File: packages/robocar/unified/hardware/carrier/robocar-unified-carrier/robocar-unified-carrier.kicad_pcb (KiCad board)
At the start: 2 copper layers, 100 x 100 mm, 38 parts, among them J1 IDC 2x7 head cable, J10 Piezo, J2 IDC 2x7 head cable, J3 XT30 pack in, J4 LM2596 module, J5 Motor left, J6 Motor right, J7 RCWL-1601 front, J8 RCWL-1601 rear, J9 SSD1306 0.91in, U1 XIAO ESP32-S3 Sense, U2 AMS1117-3.3

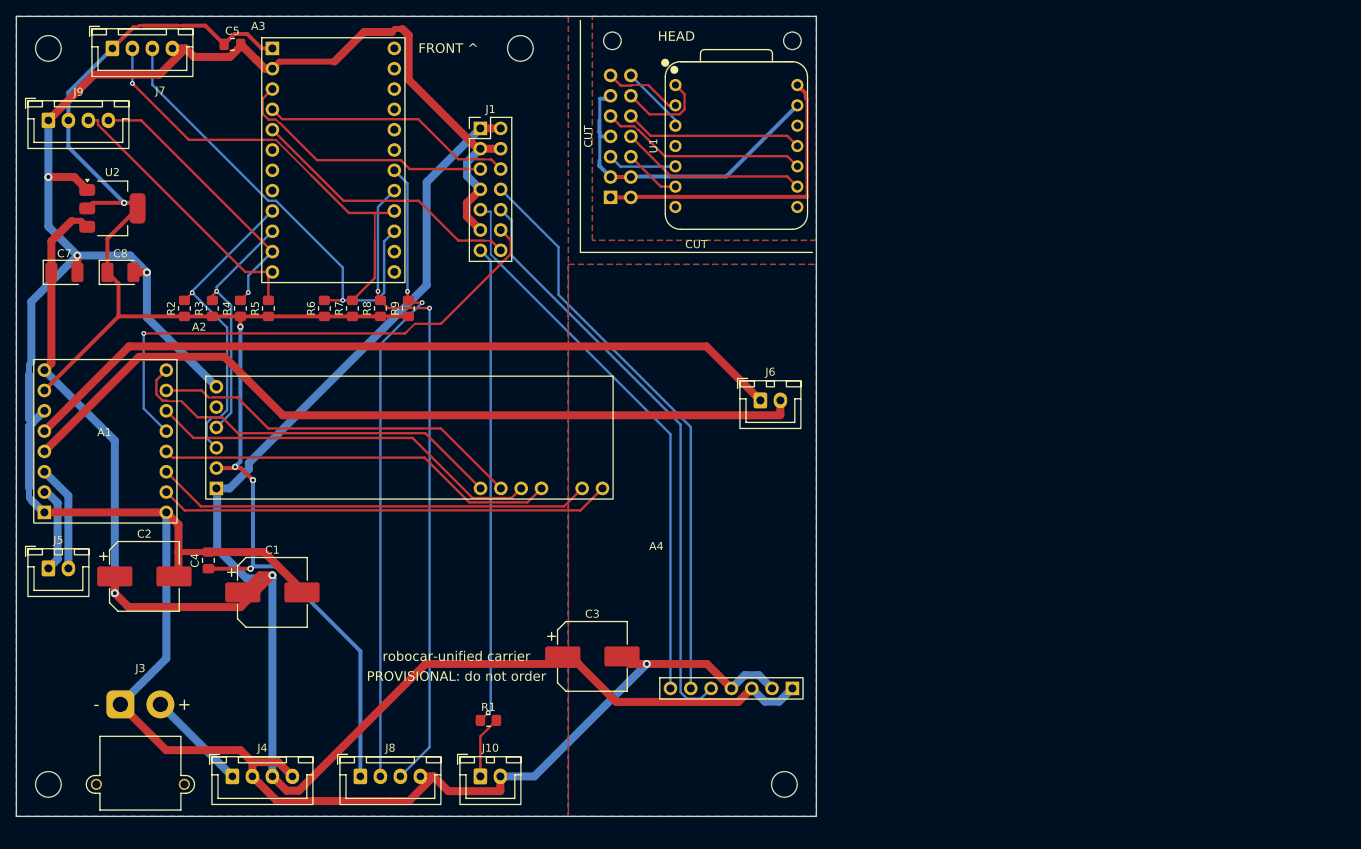
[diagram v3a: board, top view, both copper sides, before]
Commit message: feat(robocar-unified): carrier pre-order changes and three-head panel (#802)
* feat(kicad): circular board cutouts from board.toml [[cutouts]]

robocar-unified's head is sawn off the main board along an L-shaped line
(#750), and a hand saw cannot turn a sharp inside corner: the blade binds and
the corner cracks. A small hole at the corner gives the blade room to turn,
so board.toml needs a way to put a hole through the board. Its copper keepout
band forbids footprints, so the hole is board geometry, not a part.

- board.toml [[cutouts]]: { name, center = [x, y], diameter }, positions
  relative to the outline's top-left corner. boardcheck rejects a missing or
  repeated name, a bad centre or diameter, unknown keys, and a circle that
  is not strictly inside the outline (one touching it would open the edge).
- boardinput passes them through; build_board.py draws each as a circle on
  Edge.Cuts. KiCad's Specctra export then carries the hole as a keepout
  polygon on every signal layer, with the boundary still the outline
  rectangle, so Freerouting routes around it; a test pins both, and fails
  with the drawing removed.

balancebot's board.toml has no cutouts: its DSN export still equals the
fixture.

Co-Authored-By: Claude Opus 5.5 <noreply@anthropic.com>
Claude-Session: https://claude.ai/code/session_01LmLtwHDbHDLXFMLxCn3smf

* feat(parts): reversal-safe head ribbon pinout, UART0 TX carried to a tap

The head ribbon plugs onto unshrouded 2x7 pin headers, so its IDC plug also
fits rotated 180 degrees, which takes pin n to pin 15 - n. With the old
order that put 5 V on XIAO GPIOs. The new order (Lauri, 2026-10-16) pairs
each pin with one that is safe to swap with it:

  (1,14) 5V/5V  (2,13) GND/GND  (3,12) BCLK/LRC  (4,11) STBY/MUX_RST
  (5,10) SCL/SDA  (6,9) UART0 TX/NC  (7,8) DIN/PIEZO

Every non-I2C signal is a XIAO output driving a main-board input, so a
reversed plug only swaps outputs between inputs; I2C swaps with itself, and
TX lands on the unconnected pin 9.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
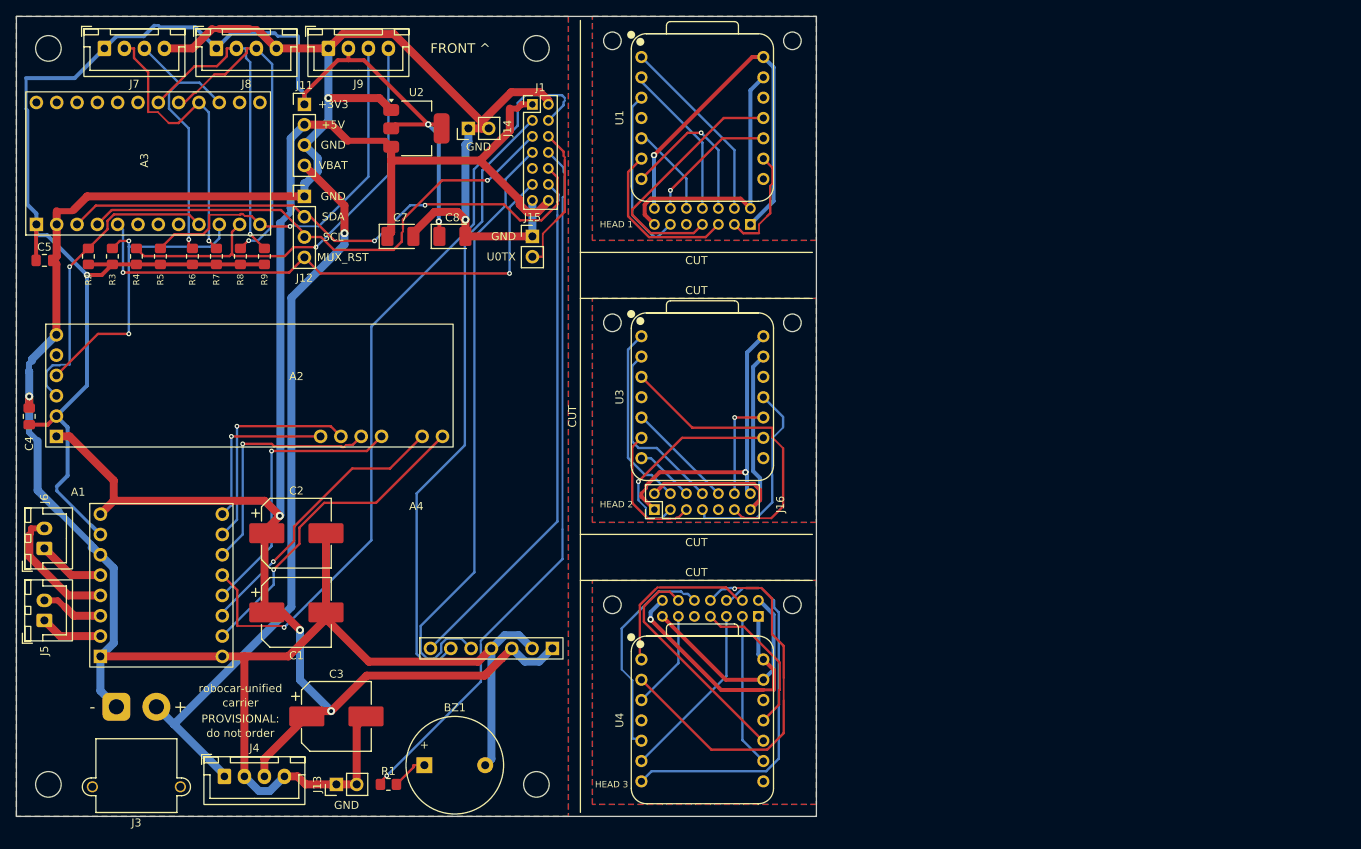
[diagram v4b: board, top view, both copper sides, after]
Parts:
- removed J10: Piezo, Connector_JST:JST_XH_B2B-XH-A_1x02_P2.50mm_Vertical
- added BZ1: Buzzer 12mm, Buzzer_Beeper:Buzzer_12x9.5RM7.6, F.Cu at (151.0, 193.6)
- added H10: M2, MountingHole:MountingHole_2.2mm_M2_ISO7380, F.Cu at (197.0, 173.6)
- added H7: M2, MountingHole:MountingHole_2.2mm_M2_ISO7380, F.Cu at (174.5, 138.3)
- added H8: M2, MountingHole:MountingHole_2.2mm_M2_ISO7380, F.Cu at (197.0, 138.3)
- added H9: M2, MountingHole:MountingHole_2.2mm_M2_ISO7380, F.Cu at (174.5, 173.6)
- added J11: Test: 3V3 5V GND VBAT, Connector_PinHeader_2.54mm:PinHeader_1x04_P2.54mm_Vertical, F.Cu at (136.0, 111.0)
- added J12: Test: GND SDA SCL RST, Connector_PinHeader_2.54mm:PinHeader_1x04_P2.54mm_Vertical, F.Cu at (136.0, 122.5)
- added J13: GND post, Connector_PinHeader_2.54mm:PinHeader_1x02_P2.54mm_Vertical, F.Cu at (140.0, 196.0)
- added J14: GND post, Connector_PinHeader_2.54mm:PinHeader_1x02_P2.54mm_Vertical, F.Cu at (156.5, 114.0)
- added J15: UART0 TX tap, Connector_PinHeader_2.54mm:PinHeader_1x02_P2.54mm_Vertical, F.Cu at (164.5, 127.5)
- added J16: IDC 2x7 head cable, Connector_PinHeader_2.00mm:PinHeader_2x07_P2.00mm_Vertical, F.Cu at (179.8, 161.7)
- added J17: IDC 2x7 head cable, Connector_PinHeader_2.00mm:PinHeader_2x07_P2.00mm_Vertical, B.Cu at (192.8, 175.0)
- added U3: XIAO ESP32-S3 Sense, Seeed_XIAO:XIAO-ESP32-S3-Socket, F.Cu at (185.8, 147.6)
- added U4: XIAO ESP32-S3 Sense, Seeed_XIAO:XIAO-ESP32-S3-Socket, F.Cu at (185.8, 188.0)
- H5, H6: footprint MountingHole:MountingHole_2.2mm_M2 -> MountingHole:MountingHole_2.2mm_M2_ISO7380
- J1, J2: footprint Connector_PinHeader_2.54mm:PinHeader_2x07_P2.54mm_Vertical -> Connector_PinHeader_2.00mm:PinHeader_2x07_P2.00mm_Vertical
- moved J8 92.8 mm to (125.0, 104.0)
- moved J6 91.4 mm to (103.5, 166.5), turned to 90 degrees
- moved C7 42.2 mm to (148.0, 127.5)
- moved C8 41.7 mm to (154.5, 127.5)
- moved U2 39.3 mm to (150.0, 114.0)
- moved A3 36.8 mm to (102.5, 126.0), turned to 90 degrees
- moved J9 36.1 mm to (139.0, 104.0)
- moved C5 35.8 mm to (103.5, 130.5)
- moved C3 32.9 mm to (140.0, 187.5)
- moved H4 31.0 mm to (165.0, 196.0)
- moved A4 30.4 mm to (167.0, 179.0)
- moved C4 28.7 mm to (101.6, 150.0)
- moved A2 21.0 mm to (105.0, 152.5)
- moved C2 19.8 mm to (135.0, 164.6)
- moved A1 19.3 mm to (110.5, 180.0)
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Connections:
- J1 pad 10: I2S_DIN -> I2C_SDA
- J1 pad 11: GND -> MUX_RST
- J1 pad 12: MOTOR_STBY -> I2S_LRCLK
- J1 pad 13: PIEZO -> GND
- J1 pad 14: MUX_RST -> +5V
- J1 pad 2: +5V -> GND
- J1 pad 3: GND -> I2S_BCLK
- J1 pad 4: GND -> MOTOR_STBY
- J1 pad 5: I2C_SDA -> I2C_SCL
- J1 pad 6: I2C_SCL -> UART0_TX
- J1 pad 7: GND -> I2S_DIN
- J1 pad 8: I2S_BCLK -> PIEZO
- J1 pad 9: I2S_LRCLK -> unconnected-(J1-Pin_9-Pad9)
- J2 pad 10: HEAD_I2S_DIN -> HEAD_I2C_SDA
- J2 pad 11: HEAD_GND -> HEAD_MUX_RST
- J2 pad 12: HEAD_MOTOR_STBY -> HEAD_I2S_LRCLK
- J2 pad 13: HEAD_PIEZO -> HEAD_GND
- J2 pad 14: HEAD_MUX_RST -> HEAD_+5V
- J2 pad 2: HEAD_+5V -> HEAD_GND
- J2 pad 3: HEAD_GND -> HEAD_I2S_BCLK
- J2 pad 4: HEAD_GND -> HEAD_MOTOR_STBY
- J2 pad 5: HEAD_I2C_SDA -> HEAD_I2C_SCL
- J2 pad 6: HEAD_I2C_SCL -> HEAD_UART0_TX
- J2 pad 7: HEAD_GND -> HEAD_I2S_DIN
- J2 pad 8: HEAD_I2S_BCLK -> HEAD_PIEZO
- J2 pad 9: HEAD_I2S_LRCLK -> unconnected-(J2-Pin_9-Pad9)
- U1 pad 7: unconnected-(U1-D6-Pad7) -> HEAD_UART0_TX
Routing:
- net MOT_A01: track 96.7 -> 8.38 mm
- net MOT_A02: track 101.8 -> 16.2 mm
- net VBAT: track 12.7 -> 93.0 mm, vias 0 -> 1
- net HEAD3_PIEZO: track 0.00 -> 48.6 mm, vias 0 -> 1
- net HEAD3_UART0_TX: track 0.00 -> 45.6 mm
- net +5V: track 264.6 -> 219.0 mm, vias 2 -> 3
- net CH4_SDA: track 81.3 -> 41.0 mm, vias 2 -> 1
- net CH4_SCL: track 80.2 -> 40.3 mm, vias 2 -> 1
- net HEAD2_+5V: track 0.00 -> 37.9 mm, vias 0 -> 1
- net I2C_SDA: track 33.7 -> 71.4 mm, vias 0 -> 2
- net HEAD2_GND: track 0.00 -> 37.5 mm
- net HEAD2_MUX_RST: track 0.00 -> 36.5 mm
- net MOTOR_STBY: track 66.9 -> 100.8 mm
- net MUX_RST: track 34.8 -> 68.5 mm, vias 0 -> 2
- net I2C_SCL: track 31.6 -> 64.9 mm, vias 0 -> 1
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- added copper zone on B.Cu, net HEAD2_GND
- added copper zone on F.Cu, net HEAD2_GND
- added copper zone on B.Cu, net HEAD3_GND
- added copper zone on F.Cu, net HEAD3_GND
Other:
- board text added: "+3V3"
- board text added: "+5V"
- board text added: "GND"
- board text added: "HEAD 1"
- board text added: "HEAD 2"
- board text added: "HEAD 3"
- board text added: "MUX_RST"
- board text added: "PROVISIONAL:"
- board text added: "SCL"
- board text added: "SDA"
- board text added: "U0TX"
- board text added: "VBAT"
- board text added: "carrier"
- board text added: "do not order"
- board text added: "robocar-unified"
- board text removed: "HEAD"
- board text removed: "PROVISIONAL: do not order"
- board text removed: "robocar-unified carrier"

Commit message: feat(robocar-unified): MCP23017 socket and GPIO mirror header on the carrier
Lauri asked for the CJMCU-2317 module on the main board, socketed by all 30
holes, with a 2x10 header repeating its GPIO column for jumpers
(2026-10-16). A5 sits on TCA9548A channel 2 with its own 10 kΩ pull-ups
(R10, R11); A0-A2 go straight to GND, so it answers at 0x20 (MCP23017_ADDR)
whatever the module's own bias, and RESET goes straight to 3V3. J18
carries EXP_INTA/INTB and EXP_GPA0-GPB7 in the module's own order. The
expander part is now in both views; its harness entries are unchanged, and
`just hardware::gen` leaves every harness output as it was. SD2/SC2 leave
the TCA9548A socket's no_connect list.

The main board had no 28 x 27 mm gap, so parts moved within the 100 x
100 mm panel. A5 (turned 180 degrees, its I2C column toward the mux) and
J18 take the right of the band below the front row, where the regulator
group, the ribbon end and the UART tap were. J1 and J15 move into the front
row, the regulator group (U2, C7, C8, J14) between the bulk capacitors and
the amplifier, and the OLED lead into the rear row. The PCA9685 and the
row below it move down 1.3 and 0.6 mm. J5/J6, J7/J8 and J3/J4 stay
together, J13 moves next to the amplifier, J14 stays by the regulator, and
the head column is not moved. Freerouting re-routed the whole panel; the
tracks are still unreviewed and the board stays PROVISIONAL.

Co-Authored-By: Claude Opus 5.5 <noreply@anthropic.com>
Claude-Session: https://claude.ai/code/session_01LmLtwHDbHDLXFMLxCn3smf
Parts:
- added A5: CJMCU-2317, Breakout_Sockets:CJMCU_2317_Socket, F.Cu at (160.7, 132.7)
- added J18: GPIO A/B, Connector_PinHeader_2.54mm:PinHeader_2x10_P2.54mm_Vertical, F.Cu at (167.0, 132.7)
- added R10: 10k, Resistor_SMD:R_0805_2012Metric_Pad1.20x1.40mm_HandSolder, F.Cu at (134.4, 133.3)
- added R11: 10k, Resistor_SMD:R_0805_2012Metric_Pad1.20x1.40mm_HandSolder, F.Cu at (138.4, 133.3)
- moved J9 82.5 mm to (125.3, 185.4)
- moved J14 68.4 mm to (144.0, 181.2)
- moved U2 56.8 mm to (145.6, 170.6), turned to 90 degrees
- moved C8 50.3 mm to (145.6, 177.0)
- moved C7 36.0 mm to (145.6, 163.4)
- moved J15 27.7 mm to (153.0, 102.3)
- moved J1 27.5 mm to (137.5, 106.0), turned to 90 degrees
- moved J13 15.0 mm to (150.5, 185.3)
- moved C3 2.00 mm to (142.0, 187.5)
- moved J11 2.00 mm to (134.0, 111.0)
- moved J12 2.00 mm to (134.0, 122.5)
- moved A2 1.30 mm to (105.0, 153.8)
- moved C4 1.30 mm to (101.6, 151.3)
- moved A1 0.60 mm to (110.5, 180.6)
- moved C1 0.60 mm to (135.0, 175.1)
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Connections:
- A3 pad 13: unconnected-(A3-Pin_13-Pad13) -> CH2_SDA
- A3 pad 14: unconnected-(A3-Pin_14-Pad14) -> CH2_SCL
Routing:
- net +5V: track 219.0 -> 284.3 mm, vias 3 -> 4
- net PIEZO: track 89.4 -> 142.1 mm, vias 1 -> 6
- net +3V3: track 192.4 -> 245.0 mm, vias 3 -> 1
- net CH2_SDA: track 0.00 -> 50.0 mm, vias 0 -> 2
- net GND: track 354.5 -> 401.7 mm, vias 3 -> 1
- net CH2_SCL: track 0.00 -> 44.1 mm, vias 0 -> 2
- net I2S_LRCLK: track 65.2 -> 107.8 mm
- net CH1_SDA: track 56.2 -> 89.5 mm, vias 1 -> 2
- net CH1_SCL: track 48.1 -> 77.4 mm, vias 1 -> 2
- net HEAD2_I2S_BCLK: track 26.4 -> 45.9 mm
- net BIN2: track 35.5 -> 51.6 mm
- net PWMB: track 40.2 -> 53.0 mm
- net MUX_RST: track 68.5 -> 58.0 mm, vias 2 -> 0
- net I2C_SDA: track 71.4 -> 62.1 mm
- net MOTOR_STBY: track 100.8 -> 109.5 mm, vias 1 -> 3
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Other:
- board text added: "3V3"
- board text added: "A"
- board text added: "B"

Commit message: fix(robocar-unified): mark which face of the CJMCU-2317 goes up
The module also fits its socket face down, flipped top to bottom: its
three columns still land on the same x positions, rows reversed. That
puts its VCC on a GND pad and SDA and A2 on 3V3 pads, which feeds the
3V3 rail through the MCP23017's ESD clamps. Its labels are printed only on
its back, and the square pad hides under the header, so nothing on the
board said which way it goes.

The silkscreen now says "CHIP SIDE UP / LABELS FACE DOWN" under A5. Inside
the socket outline it names every single-column pin and each
double-column row ("B0 A0" ... "VCC GND"), which stays visible with the
headers fitted. J18 has no room for row labels (0.67 mm to the board
edge, 1.1 mm to A5's header); its rows line up with A5's. The J1 comment
now gives its distance to the head column: Lauri's "10-15 cm reaches"
was about its old spot and needs confirming. The board was re-placed,
re-routed and re-checked.

Co-Authored-By: Claude Opus 5.5 <noreply@anthropic.com>
Claude-Session: https://claude.ai/code/session_01LmLtwHDbHDLXFMLxCn3smf
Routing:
- net +5V: track 284.3 -> 221.2 mm
- net PIEZO: track 142.1 -> 114.3 mm, vias 6 -> 1
- net I2S_LRCLK: track 107.8 -> 82.6 mm, vias 0 -> 3
- net GND: track 401.7 -> 387.1 mm, vias 1 -> 2
- net I2C_SDA: track 62.1 -> 73.8 mm, vias 2 -> 4
- net MOTOR_STBY: track 109.5 -> 101.8 mm, vias 3 -> 6
- net VBAT: track 98.8 -> 93.0 mm, vias 3 -> 4
- net CH2_SCL: track 44.1 -> 38.4 mm, vias 2 -> 3
- net CH2_SDA: track 50.0 -> 55.5 mm, vias 2 -> 1
- net MUX_RST: track 58.0 -> 59.4 mm
- net CH1_SCL: track 77.4 -> 78.6 mm, vias 2 -> 3
- net CH1_SDA: track 89.5 -> 88.5 mm
- net UART0_TX: track 18.6 -> 19.4 mm, vias 0 -> 1
- net I2C_SCL: track 60.2 -> 60.4 mm, vias 0 -> 1
- net I2S_DIN: track 78.6 -> 78.8 mm, vias 1 -> 2
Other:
- board text added: "A0"
- board text added: "A1"
- board text added: "A2"
- board text added: "B0 A0"
- board text added: "B1 A1"
- board text added: "B2 A2"
- board text added: "B3 A3"
- board text added: "B4 A4"
- board text added: "B5 A5"
- board text added: "B6 A6"
- board text added: "B7 A7"
- board text added: "CHIP SIDE UP"
- board text added: "INTB INTA"
- board text added: "LABELS FACE DOWN"
- board text added: "NC"
- board text added: "RST"
- board text added: "VCC"
- board text added: "VCC GND"

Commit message: fix(robocar-unified): stop the head pours 1 mm short of the cut lines
HEAD2_GND and HEAD3_GND poured right up to the y 35.25 and y 70.5 saw
lines, where the hand saw's kerf and the board's flex can bridge their
copper. Both regions now start 1 mm in; the keepout bands are unchanged
(widening them blocked two routes near J17). Board re-routed and every
carrier gate passed. Part of #810.

Co-Authored-By: Claude Opus 5.5 <noreply@anthropic.com>
Claude-Session: https://claude.ai/code/session_01AoNL8UeiSeWCVt1Bs1JLVr
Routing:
- net GND: track 387.1 -> 397.0 mm, vias 2 -> 1
